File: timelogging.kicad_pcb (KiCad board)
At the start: 2 copper layers, 82.5 x 49.5 mm, 40 parts, among them J1 Micro_SD_Card, J2 ICSP, J3 RTC_ICSP, Q1 2N7002, Q2 16Mhz, SW1 SW_A, SW2 SW_B, U1 RP402, U2 ATMEGA328P-PU, U3 DS3231

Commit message: improve power circuit
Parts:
- moved C1 12.7 mm to (53.8, 92.6), turned to 90 degrees
- moved C2 8.31 mm to (59.5, 92.6), turned to 90 degrees
- moved L1 6.74 mm to (57.0, 85.6), turned to 180 degrees
- moved U1 6.18 mm to (56.7, 90.9), turned to 270 degrees
- moved R12 0.51 mm to (59.4, 78.2)
- moved R14 0.51 mm to (52.8, 78.2)
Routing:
- net GND: track 76.4 -> 68.3 mm
- net VCC: track 182.0 -> 174.2 mm, vias 10 -> 9
- net Net-(R12-Pad1): track 23.4 -> 22.8 mm
- net Net-(BAT_VCC1-Pad1): track 26.2 -> 26.6 mm, vias 0 -> 2
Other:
- board text added: "+"
- board text added: "-"
- board text added: "GND"
- board text added: "MISO"
- board text added: "MOSI"
- board text added: "RST"
- board text added: "SCK"
- board text added: "SCL"
- board text added: "SDA"

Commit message: rework schematic
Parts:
- moved C1 1.84 mm to (52.1, 91.9)
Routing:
- net GND: track 68.3 -> 79.9 mm, vias 13 -> 10
- net Net-(BAT_VCC1-Pad1): track 26.6 -> 27.5 mm, vias 2 -> 3
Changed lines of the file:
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@@
     (links 93)
     (no_connects 0)
-    (area 44.374999 62.154999 127.075001 111.835001)
+    (area 38.702857 61.865 132.747143 112.225)
     (thickness 1.6)
     (drawings 15)
-    (tracks 381)
+    (tracks 380)
     (zones 0)
     (modules 40)
@@
     (visible_elements 7FFFFFFF)
     (pcbplotparams
-      (layerselection 0x00030_80000001)
+      (layerselection 0x010f0_80000001)
       (usegerberextensions false)
       (excludeedgelayer true)
@@
       (outputformat 1)
       (mirror false)
-      (drillshape 1)
+      (drillshape 0)
       (scaleselection 1)
-      (outputdirectory ""))
+      (outputdirectory gerber/))
   )
   (net 0 "")
@@
   )
   (module Capacitors_SMD:C_0603_HandSoldering (layer F.Cu)
-    (at 53.7972 92.583 90)
+    (at 52.07 91.948 90)
     (descr "Capacitor SMD 0603, hand soldering")
     (tags "capacitor 0603")
@@
   (gr_line (start 127 62.23) (end 127 111.76) (angle 90) (layer Edge.Cuts) (width 0.15))
   (gr_line (start 44.45 62.23) (end 127 62.23) (angle 90) (layer Edge.Cuts) (width 0.15))
-  (segment (start 57.023 90.932) (end 55.753 90.932) (width 0.25) (layer F.Cu) (net 1))
-  (via (at 52.197 90.932) (size 0.6) (drill 0.4) (layers F.Cu B.Cu) (net 1))
-  (segment (start 55.753 90.932) (end 52.197 90.932) (width 0.25) (layer B.Cu) (net 1))
-  (via (at 55.753 90.932) (size 0.6) (drill 0.4) (layers F.Cu B.Cu) (net 1))
+  (segment (start 91.694 84.582) (end 90.932 83.82) (width 0.25) (layer B.Cu) (net 1))
+  (via (at 77.47 83.82) (size 0.6) (drill 0.4) (layers F.Cu B.Cu) (net 1))
+  (segment (start 90.932 83.82) (end 77.47 83.82) (width 0.25) (layer B.Cu) (net 1))
+  (segment (start 56.7182 89.582) (end 56.7182 90.6018) (width 0.25) (layer F.Cu) (net 1))
+  (segment (start 56.322 90.998) (end 52.07 90.998) (width 0.25) (layer F.Cu) (net 1))
+  (segment (start 56.7182 90.6018) (end 56.322 90.998) (width 0.25) (layer F.Cu) (net 1))
   (segment (start 56.7182 89.582) (end 56.7182 90.6272) (width 0.25) (layer F.Cu) (net 1))
   (segment (start 58.8112 90.932) (end 59.5122 91.633) (width 0.25) (layer F.Cu) (net 1))
   (segment (start 57.023 90.932) (end 58.8112 90.932) (width 0.25) (layer F.Cu) (net 1))
   (segment (start 56.7182 90.6272) (end 57.023 90.932) (width 0.25) (layer F.Cu) (net 1))
-  (segment (start 59.5122 91.633) (end 59.5122 90.7288) (width 0.25) (layer F.Cu) (net 1))
-  (via (at 62.23 89.916) (size 0.6) (drill 0.4) (layers F.Cu B.Cu) (net 1))
-  (segment (start 60.325 89.916) (end 62.23 89.916) (width 0.25) (layer B.Cu) (net 1))
-  (via (at 60.325 89.916) (size 0.6) (drill 0.4) (layers F.Cu B.Cu) (net 1))
-  (segment (start 59.5122 90.7288) (end 60.325 89.916) (width 0.25) (layer F.Cu) (net 1))
   (segment (start 103.378 77.216) (end 101.854 77.216) (width 0.25) (layer B.Cu) (net 1))
   (segment (start 98.933 74.295) (end 99.06 74.422) (width 0.25) (layer F.Cu) (net 1))
@@
   (segment (start 79.248 92.456) (end 90.424 92.456) (width 0.25) (layer F.Cu) (net 19))
   (segment (start 75.645 86.995) (end 75.645 88.9) (width 0.25) (layer F.Cu) (net 19) (status 30))
-  (segment (start 53.7972 93.533) (end 53.7972 93.2688) (width 0.25) (layer F.Cu) (net 21))
-  (segment (start 53.7972 93.2688) (end 54.61 92.456) (width 0.25) (layer F.Cu) (net 21))
-  (segment (start 54.7222 88.6608) (end 54.7222 85.598) (width 0.25) (layer F.Cu) (net 21))
-  (segment (start 54.61 88.773) (end 54.7222 88.6608) (width 0.25) (layer F.Cu) (net 21))
-  (via (at 54.61 88.773) (size 0.6) (drill 0.4) (layers F.Cu B.Cu) (net 21))
-  (segment (start 54.61 90.297) (end 54.61 88.773) (width 0.25) (layer B.Cu) (net 21))
-  (via (at 54.61 90.297) (size 0.6) (drill 0.4) (layers F.Cu B.Cu) (net 21))
-  (segment (start 54.61 92.456) (end 54.61 90.297) (width 0.25) (layer F.Cu) (net 21))
+  (segment (start 55.7682 92.282) (end 54.944 92.282) (width 0.25) (layer F.Cu) (net 21))
+  (segment (start 54.7222 88.5338) (end 54.7222 85.598) (width 0.25) (layer F.Cu) (net 21))
+  (segment (start 54.356 88.9) (end 54.7222 88.5338) (width 0.25) (layer F.Cu) (net 21))
+  (via (at 54.356 88.9) (size 0.6) (drill 0.4) (layers F.Cu B.Cu) (net 21))
+  (segment (start 54.356 91.694) (end 54.356 88.9) (width 0.25) (layer B.Cu) (net 21))
+  (segment (start 54.61 91.948) (end 54.356 91.694) (width 0.25) (layer B.Cu) (net 21))
+  (via (at 54.61 91.948) (size 0.6) (drill 0.4) (layers F.Cu B.Cu) (net 21))
+  (segment (start 54.944 92.282) (end 54.61 91.948) (width 0.25) (layer F.Cu) (net 21))
+  (segment (start 52.07 92.898) (end 55.1522 92.898) (width 0.25) (layer F.Cu) (net 21))
+  (segment (start 55.1522 92.898) (end 55.7682 92.282) (width 0.25) (layer F.Cu) (net 21))
+  (segment (start 66.294 94.234) (end 62.865 94.234) (width 0.25) (layer B.Cu) (net 21))
+  (segment (start 62.865 94.234) (end 62.23 94.869) (width 0.25) (layer B.Cu) (net 21))
+  (segment (start 62.23 94.869) (end 56.261 94.869) (width 0.25) (layer B.Cu) (net 21))
+  (via (at 56.261 94.869) (size 0.6) (drill 0.4) (layers F.Cu B.Cu) (net 21))
+  (segment (start 56.261 94.869) (end 55.7682 94.3762) (width 0.25) (layer F.Cu) (net 21))
+  (segment (start 55.7682 94.3762) (end 55.7682 92.282) (width 0.25) (layer F.Cu) (net 21))
+  (segment (start 52.07 92.898) (end 52.07 92.6338) (width 0.25) (layer F.Cu) (net 21) (status 30))
   (segment (start 55.7682 92.282) (end 55.7682 91.5822) (width 0.25) (layer F.Cu) (net 21))
-  (segment (start 66.294 94.234) (end 61.214 94.234) (width 0.25) (layer F.Cu) (net 21))
-  (segment (start 55.7682 94.2492) (end 55.7682 92.282) (width 0.25) (layer F.Cu) (net 21))
-  (segment (start 56.896 95.377) (end 55.7682 94.2492) (width 0.25) (layer F.Cu) (net 21))
-  (segment (start 60.071 95.377) (end 56.896 95.377) (width 0.25) (layer F.Cu) (net 21))
-  (segment (start 61.214 94.234) (end 60.071 95.377) (width 0.25) (layer F.Cu) (net 21))
-  (segment (start 53.7972 93.533) (end 54.5172 93.533) (width 0.25) (layer F.Cu) (net 21))
-  (segment (start 54.5172 93.533) (end 55.7682 92.282) (width 0.25) (layer F.Cu) (net 21))
   (segment (start 54.7222 85.598) (end 54.7222 87.213) (width 0.25) (layer F.Cu) (net 21) (status 30))
   (segment (start 88.714 88.144) (end 85.271 88.144) (width 0.25) (layer F.Cu) (net 22) (status 30))

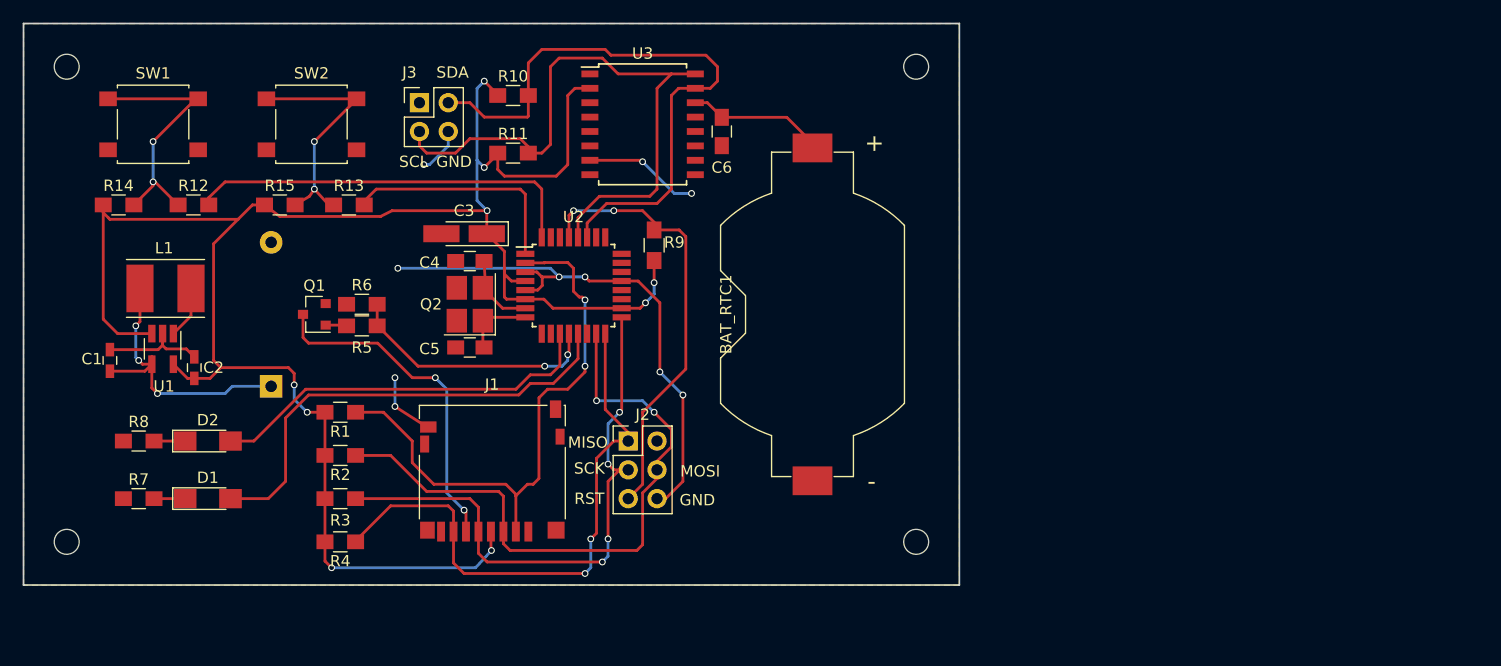
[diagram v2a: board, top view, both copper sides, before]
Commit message: redo pcb design
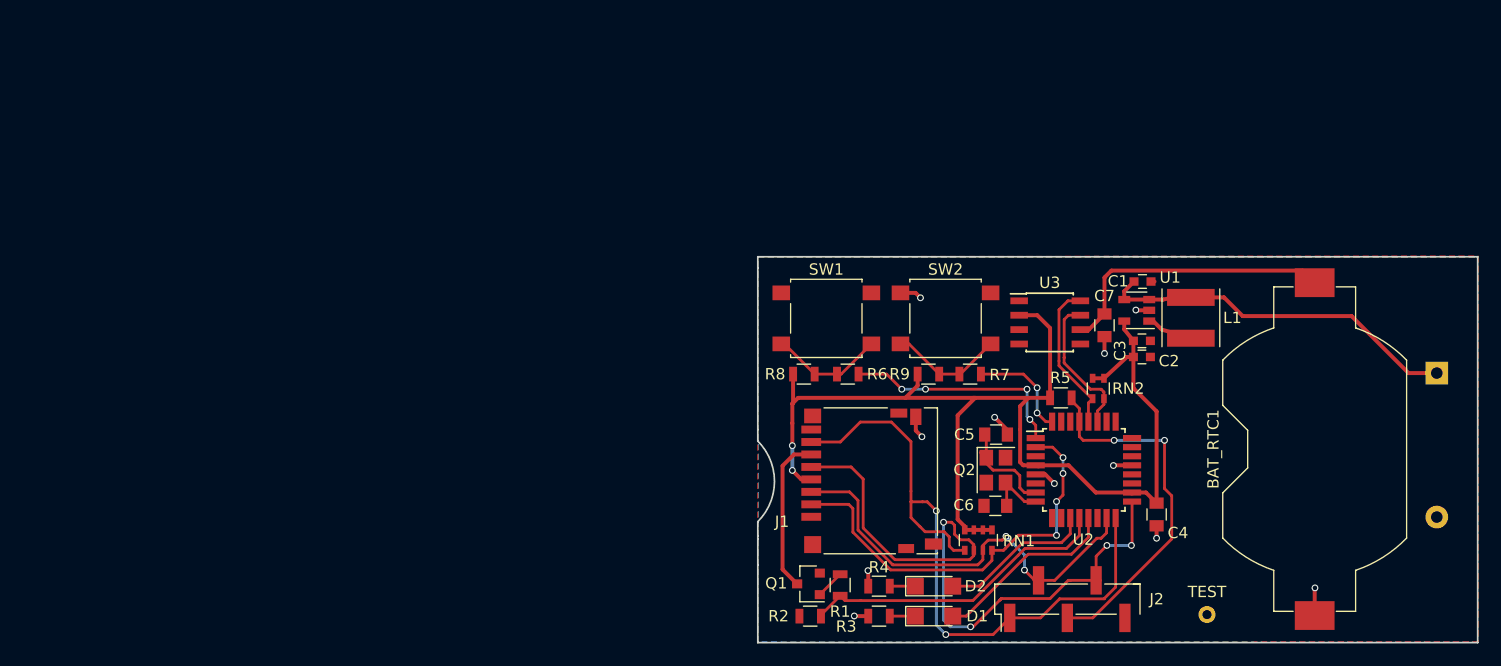
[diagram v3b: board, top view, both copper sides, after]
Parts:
- removed J3: RTC_ICSP, Pin_Headers:Pin_Header_Straight_2x02_Pitch2.54mm
- removed R10, R11, R14, R15: 10K, Resistors_SMD:R_0805_HandSoldering
- removed R12, R13: 1K, Resistors_SMD:R_0805_HandSoldering
- removed REF** (x4): MountingHole_2.2mm_M2, Mounting_Holes:MountingHole_2.2mm_M2
- added C7: 10uF, Capacitors_SMD:C_0805, F.Cu at (139.8, 88.8)
- added RN1: 10K, Resistors_SMD:R_Array_Convex_4x0603, F.Cu at (128.7, 107.8)
- added RN2: 10K, Resistors_SMD:R_Array_Convex_2x0603, F.Cu at (139.3, 94.4)
- added TEST: Measurement_Point_Round-TH_Small, Measurement_Points:Measurement_Point_Round-TH_Small, F.Cu at (148.8, 114.4)
- BAT_VCC1: footprint Battery_Holders:Keystone_2468_2xAAA -> battery_holder:Keystone_2468_2xAAA
- C1, C2: footprint Capacitors_SMD:C_0603_HandSoldering -> Capacitors_SMD:C_0603
- C3: value 0.1uF -> 10uF; footprint Capacitors_Tantalum_SMD:CP_Tantalum_Case-A_EIA-3216-18_Hand -> Capacitors_SMD:C_0603
- C4: value 22pF -> 0.1uF; footprint Capacitors_SMD:C_0805_HandSoldering -> Capacitors_SMD:C_0805
- C5: footprint Capacitors_SMD:C_0805_HandSoldering -> Capacitors_SMD:C_0805
- C6: value 10uF -> 22pF; footprint Capacitors_SMD:C_0805_HandSoldering -> Capacitors_SMD:C_0805
- D1, D2: footprint LEDs:LED_1206_HandSoldering -> LEDs:LED_1206
- J2: footprint Pin_Headers:Pin_Header_Straight_2x03_Pitch2.54mm -> Pin_Headers:Pin_Header_Straight_1x05_Pitch2.54mm_SMD_Pin1Left
- L1: footprint Inductors_SMD:L_Taiyo-Yuden_NR-50xx_HandSoldering -> Inductors_SMD:L_Taiyo-Yuden_NR-50xx
- Q1: value 2N7002 -> NTR4003N
- Q2: footprint Crystals:Crystal_SMD_3225-4pin_3.2x2.5mm_HandSoldering -> Crystals:Crystal_SMD_3225-4pin_3.2x2.5mm
- R1, R3: value 10K -> 100; footprint Resistors_SMD:R_0805_HandSoldering -> Resistors_SMD:R_0805
- R2: value 10K -> 100K; footprint Resistors_SMD:R_0805_HandSoldering -> Resistors_SMD:R_0805
- R4: value 10K -> 68; footprint Resistors_SMD:R_0805_HandSoldering -> Resistors_SMD:R_0805
- R5: value 10 -> 10K; footprint Resistors_SMD:R_0805_HandSoldering -> Resistors_SMD:R_0805
- R6: value 100K -> 1K; footprint Resistors_SMD:R_0805_HandSoldering -> Resistors_SMD:R_0805
- R7: value 100 -> 1K; footprint Resistors_SMD:R_0805_HandSoldering -> Resistors_SMD:R_0805
- R8: value 68 -> 10K; footprint Resistors_SMD:R_0805_HandSoldering -> Resistors_SMD:R_0805
- R9: footprint Resistors_SMD:R_0805_HandSoldering -> Resistors_SMD:R_0805
- U1: footprint TO_SOT_Packages_SMD:SOT-23-5_HandSoldering -> TO_SOT_Packages_SMD:SOT-23-5
- U2: value ATMEGA328P-PU -> ATMEGA328PB-AU
- U3: value DS3231 -> DS3231MZ; footprint Housings_SOIC:SOIC-16W_7.5x10.3mm_Pitch1.27mm -> Housings_SOIC:SOIC-8_3.9x4.9mm_Pitch1.27mm
- moved BAT_VCC1 102.8 mm to (169.1, 93.1), turned to 180 degrees
- moved C1 91.3 mm to (143.2, 85.0), turned to 0 degrees
- moved L1 90.5 mm to (147.4, 88.2), turned to 90 degrees
- moved U1 86.0 mm to (142.6, 87.5), turned to 180 degrees
- moved C2 83.6 mm to (143.1, 91.6), turned to 0 degrees
- moved R7 74.2 mm to (128.0, 93.2)
- moved D2 65.3 mm to (124.8, 111.9)
- moved D1 64.9 mm to (124.8, 114.5)
- moved C4 64.6 mm to (144.4, 105.5), turned to 270 degrees
- moved R5 62.0 mm to (136.0, 95.2)
- moved SW1 61.8 mm to (115.3, 88.2), turned to 180 degrees
- moved C3 60.5 mm to (143.1, 90.2), turned to 0 degrees
- moved R8 59.0 mm to (113.3, 93.2)
- moved SW2 58.5 mm to (125.8, 88.2), turned to 180 degrees
- moved Q1 49.6 mm to (113.7, 111.7)
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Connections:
- C4 pad 1: GND -> VCC
- C4 pad 2: Net-(C4-Pad2) -> GND
- C6 pad 2: Net-(BAT_RTC1-Pad1) -> Net-(C6-Pad2)
- J2 pad 2: Net-(J2-Pad2) -> MOSI
- J2 pad 3: SCK -> RESET
- J2 pad 4: MOSI -> SCK
- J2 pad 5: RESET -> GND
- Q2 pad 2: Net-(C4-Pad2) -> Net-(Q2-Pad2)
- Q2 pad 3: (no net) -> Net-(C6-Pad2)
- Q2 pad 4: (no net) -> Net-(Q2-Pad4)
- R1 pad 1: CS -> Net-(Q1-Pad1)
- R1 pad 2: VCC -> SD_TOGGLE
- R2 pad 1: MOSI -> GND
- R2 pad 2: VCC -> SD_TOGGLE
- R3 pad 1: VCC -> GND
- R3 pad 2: SCK -> Net-(D1-Pad1)
- R4 pad 1: MISO -> GND
- R4 pad 2: VCC -> Net-(D2-Pad1)
- R5 pad 1: Net-(Q1-Pad1) -> VCC
- R5 pad 2: SD_TOGGLE -> RESET
- R6 pad 1: GND -> Net-(R6-Pad1)
- R6 pad 2: SD_TOGGLE -> BTN_A
- R7 pad 1: GND -> Net-(R7-Pad1)
- R7 pad 2: Net-(D1-Pad1) -> BTN_B
- R8 pad 1: GND -> VCC
- R8 pad 2: Net-(D2-Pad1) -> Net-(R6-Pad1)
- R9 pad 2: RESET -> Net-(R7-Pad1)
- SW1 pad 1: Net-(R12-Pad1) -> Net-(R6-Pad1)
- SW2 pad 1: Net-(R13-Pad1) -> Net-(R7-Pad1)
- U1 pad 3: VCC -> Net-(BAT_VCC1-Pad1)
- U2 pad 1: BTN_B -> BTN_A
- U2 pad 3: GND -> Net-(U2-Pad3)
- U2 pad 32: BTN_A -> BTN_B
- U2 pad 6: VCC -> Net-(U2-Pad6)
- U2 pad 7: Net-(C4-Pad2) -> Net-(C5-Pad2)
- U2 pad 8: Net-(C5-Pad2) -> Net-(C6-Pad2)
- U3 pad 6: GND -> Net-(BAT_RTC1-Pad1)
- U3 pad 7: GND -> SDA
- U3 pad 8: GND -> SCL
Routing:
- net VCC: track 174.2 -> 102.0 mm, vias 9 -> 2
- net GND: track 79.9 -> 18.7 mm, vias 10 -> 11
- net SCL: track 55.7 -> 13.5 mm
- net SDA: track 54.2 -> 12.9 mm
- net Net-(D1-Pad2): track 41.2 -> 16.6 mm
- net Net-(R12-Pad1): track 22.8 -> 0.00 mm, vias 2 -> 0
- net Net-(R13-Pad1): track 22.0 -> 0.00 mm, vias 2 -> 0
- net Net-(D2-Pad2): track 34.6 -> 13.7 mm
- net MOSI: track 56.2 -> 38.8 mm
- net Net-(J1-Pad6): track 29.9 -> 14.0 mm, vias 2 -> 0
- net BTN_A: track 35.1 -> 20.0 mm, vias 0 -> 4
- net CS: track 50.5 -> 37.0 mm, vias 2 -> 4
- net Net-(BAT_RTC1-Pad1): track 12.2 -> 25.2 mm
- net Net-(R7-Pad1): track 0.00 -> 11.2 mm
- net BTN_B: track 20.4 -> 9.32 mm, vias 0 -> 2
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- added copper zone on B.Cu, net GND
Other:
- board size 82.5 x 49.5 mm -> 63.5 x 34 mm
- board text removed: "+"
- board text removed: "-"
- board text removed: "GND"
- board text removed: "Leotrim Zulfiu"
- board text removed: "MISO"
- board text removed: "MOSI"
- board text removed: "RST"
- board text removed: "SCK"
- board text removed: "SCL"
- board text removed: "SDA"
